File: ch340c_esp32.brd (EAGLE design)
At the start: 10.2 x 27.7 mm, 13 parts, among them J1 CQ-USB-C16PSMT01, U1 AMS1117 3.3V, U2 CH340C, U3 AO3400, U4 AO3400

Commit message: update
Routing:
- net GND: track 0.00 -> 50.0 mm, vias 0 -> 4
- net VOUT: track 0.00 -> 22.3 mm, vias 0 -> 4
- net VIN: track 0.00 -> 21.6 mm, vias 0 -> 4
- net !RTS: track 0.00 -> 16.8 mm, vias 0 -> 2
- net !DTR: track 0.00 -> 15.8 mm
- net EN: track 0.00 -> 15.7 mm, vias 0 -> 2
- net RXD: track 0.00 -> 13.9 mm, vias 0 -> 2
- net CC1: track 0.00 -> 11.8 mm, vias 0 -> 2
- net TXD: track 0.00 -> 11.8 mm, vias 0 -> 2
- net DN1: track 0.00 -> 11.4 mm, vias 0 -> 2
- net DP1: track 0.00 -> 10.1 mm
- net IO0: track 0.00 -> 8.40 mm
- net CC2: track 0.00 -> 3.79 mm

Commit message: resolve issues
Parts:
- moved ESP32_TX 0.13 mm to (2.54, 26.4)
- moved ESP32_IO0 0.13 mm to (0.89, 26.4)
- moved ESP32_EN 0.13 mm to (5.84, 26.4)
- moved ESP32_RX 0.13 mm to (4.19, 26.4)
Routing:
- net GND: track 50.0 -> 52.6 mm
- net VIN: track 21.6 -> 22.4 mm
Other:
- board size 10.2 x 27.7 mm -> 10.2 x 27.8 mm
- board text added: "3V3"
- board text added: "5V"
- board text added: "CH340C v1.0"
- board text added: "GND"
- board text removed: "v1.0"

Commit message: prototype v1.1
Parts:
- added JP1: JUMPER-SMT_3_NO_NO-SILK, SparkFun-Jumpers:SMT-JUMPER_3_NO_NO-SILK
- C2: value 1uF -> 100nF
- moved C1 3.43 mm to (8.80, 11.9)
- moved C2 1.27 mm to (8.80, 13.8)
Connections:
- net DN1 renamed DN
- net DP1 renamed DP
- removed net NC.: U2.7
- removed net SBU1: J1.A8
- removed net SBU2: J1.B8
- removed net VIN: J1.A4_B9, J1.B4_A9, U1.3
- removed net VOUT: C1.1, U1.2, U1.4, U2.16, U2.4
- new net 3V3: JP1.1, U1.2, U1.4
- new net 5V: J1.A4_B9, J1.B4_A9, JP1.3, U1.3
- new net V3: C1.1, U2.4
- new net VCC: JP1.2, U2.16
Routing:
- net GND: track 52.6 -> 0.00 mm, vias 4 -> 0
- net VIN: track 22.4 -> 0.00 mm, vias 4 -> 0
- net VOUT: track 22.3 -> 0.00 mm, vias 4 -> 0
- net !RTS: track 16.8 -> 0.00 mm, vias 2 -> 0
- net !DTR: track 15.8 -> 0.00 mm
- net EN: track 15.6 -> 0.00 mm, vias 2 -> 0
- net RXD: track 13.8 -> 0.00 mm, vias 2 -> 0
- net TXD: track 12.0 -> 0.00 mm, vias 2 -> 0
- net CC1: track 11.8 -> 0.00 mm, vias 2 -> 0
- net DN: track 11.4 -> 0.00 mm, vias 2 -> 0
- net DP: track 10.1 -> 0.00 mm
- net IO0: track 8.27 -> 0.00 mm
- net CC2: track 3.79 -> 0.00 mm
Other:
- board size 10.2 x 27.8 mm -> 10.2 x 27.9 mm
- board text added: "JP1"

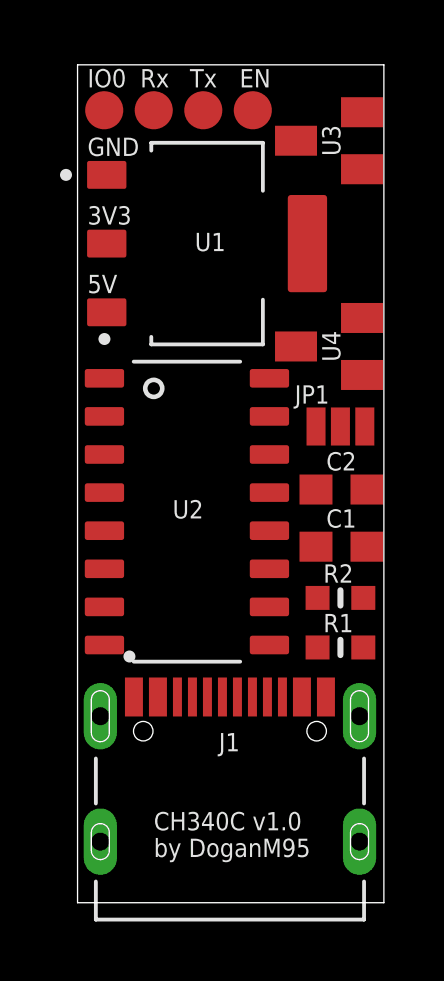
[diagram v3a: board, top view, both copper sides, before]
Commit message: route airwires for v1.1
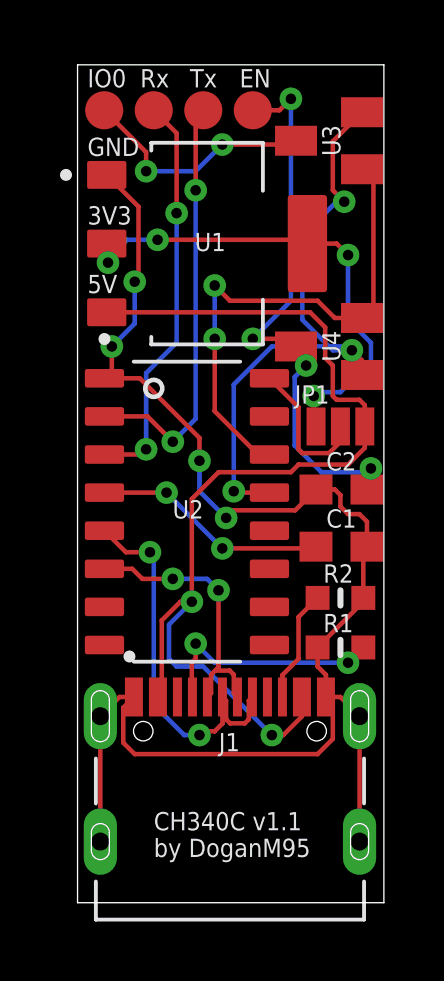
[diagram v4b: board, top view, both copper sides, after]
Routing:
- net GND: track 0.00 -> 48.7 mm, vias 0 -> 4
- net 5V: track 0.00 -> 34.9 mm, vias 0 -> 2
- net !DTR: track 0.00 -> 20.5 mm, vias 0 -> 3
- net EN: track 0.00 -> 18.8 mm, vias 0 -> 4
- net !RTS: track 0.00 -> 17.2 mm, vias 0 -> 2
- net 3V3: track 0.00 -> 16.6 mm, vias 0 -> 4
- net TXD: track 0.00 -> 14.1 mm, vias 0 -> 2
- net RXD: track 0.00 -> 13.5 mm, vias 0 -> 2
- net DP: track 0.00 -> 13.2 mm, vias 0 -> 2
- net DN: track 0.00 -> 9.28 mm, vias 0 -> 2
- net IO0: track 0.00 -> 8.03 mm, vias 0 -> 2
- net CC1: track 0.00 -> 7.90 mm, vias 0 -> 2
- net V3: track 0.00 -> 7.85 mm, vias 0 -> 2
- net VCC: track 0.00 -> 4.88 mm
- net CC2: track 0.00 -> 3.79 mm
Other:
- board text added: "CH340C v1.1"
- board text removed: "CH340C v1.0"

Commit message: update C2 cap value
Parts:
- C2: value 100nF -> 4.7uF
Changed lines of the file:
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@@
 <drawing>
 <settings>
-<setting alwaysvectorfont="yes"/>
+<setting alwaysvectorfont="no"/>
 <setting verticaltext="up"/>
 </settings>
@@
 <attribute name="VALUE" x="3.556" y="25.654" size="0.0254" layer="27"/>
 </element>
-<element name="C2" library="eagle-ltspice" library_urn="urn:adsk.eagle:library:217" package="C0603" package3d_urn="urn:adsk.eagle:package:13262/1" value="100nF" x="8.797784375" y="13.7729125" smashed="yes">
+<element name="C2" library="eagle-ltspice" library_urn="urn:adsk.eagle:library:217" package="C0603" package3d_urn="urn:adsk.eagle:package:13262/1" value="4.7uF" x="8.797784375" y="13.7729125" smashed="yes">
 <attribute name="NAME" x="8.289784375" y="14.4079125" size="0.6096" layer="25"/>
 <attribute name="SPICEMODEL" value="NONE" x="8.797784375" y="13.7729125" size="1.778" layer="27" display="off"/>
